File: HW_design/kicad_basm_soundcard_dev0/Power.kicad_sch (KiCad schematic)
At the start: 18 parts, among them J101 USB_C_Receptacle, U101 AMS1117-3.3, U102 AMS1117-3.3

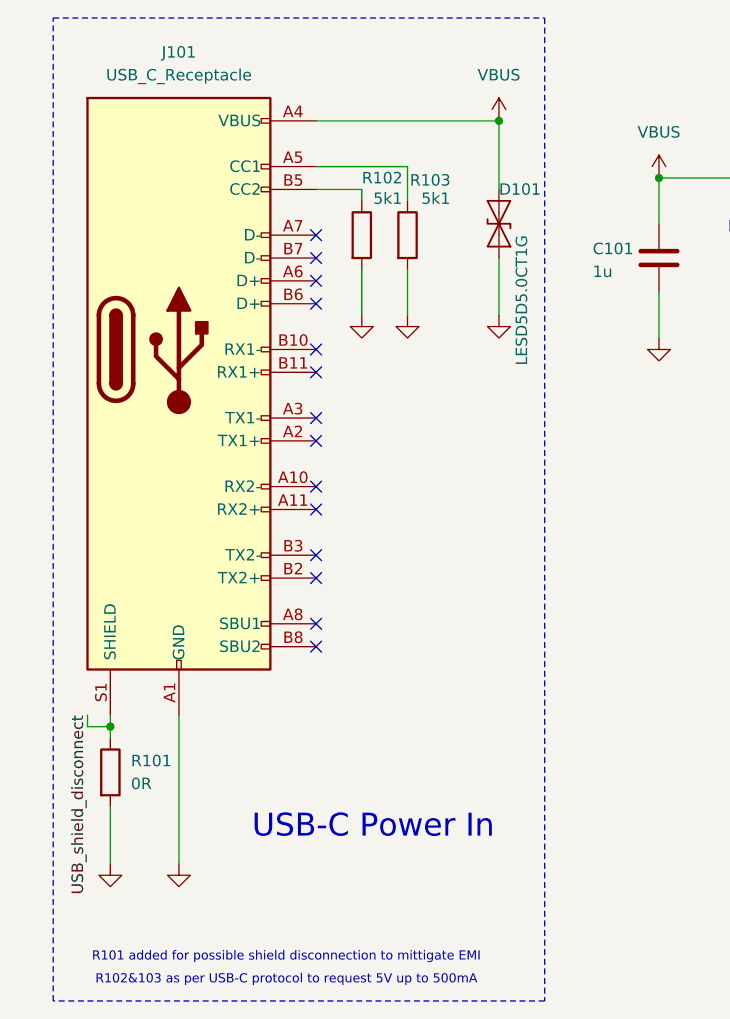
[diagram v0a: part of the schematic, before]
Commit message: Changed Footprints for LED RGB, SD, AudioJack, USB
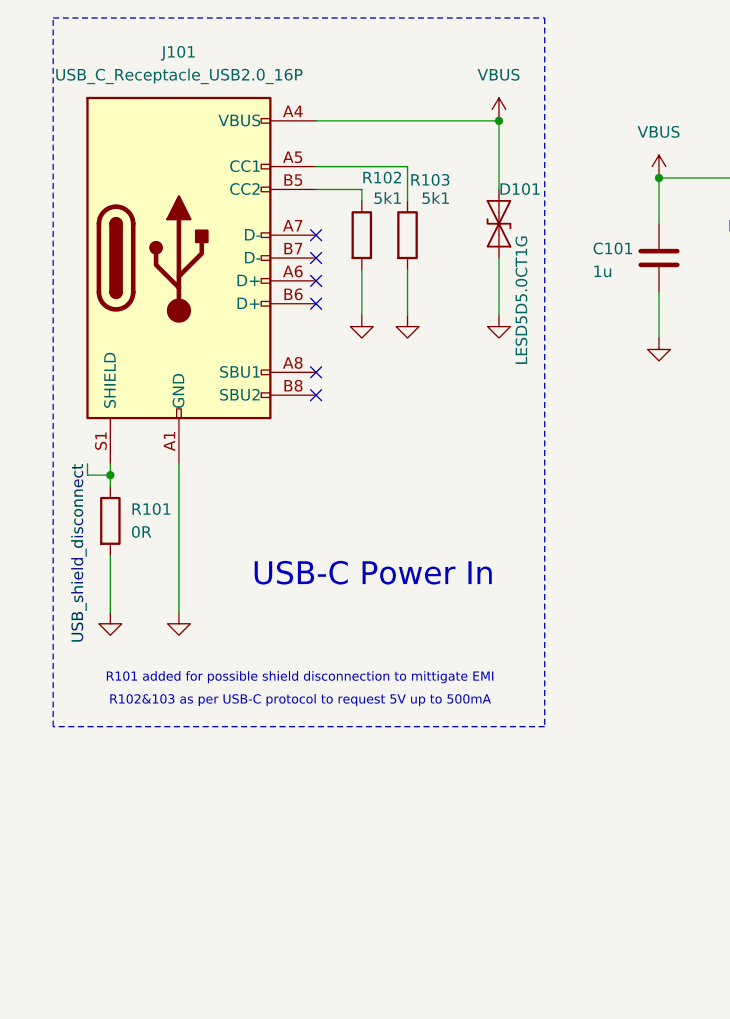
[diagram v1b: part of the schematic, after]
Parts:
- removed J101: USB_C_Receptacle, Connector_USB:USB_C_Receptacle_Molex_105450-0101, symbol Connector:USB_C_Receptacle
- added J101: USB_C_Receptacle_USB2.0_16P, Connector_USB:USB_C_Receptacle_Palconn_UTC16-G, symbol Connector:USB_C_Receptacle_USB2.0_16P
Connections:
- net GND: now also J101.A1 (GND), J101.A12 (GND), J101.B1 (GND), J101.B12 (GND)
- net USB_shield_disconnect: now also J101.S1 (SHIELD)
- net VBUS: now also J101.A4 (VBUS), J101.A9 (VBUS), J101.B4 (VBUS), J101.B9 (VBUS)
- net at R103.1: now also J101.A5 (CC1)
- net at R102.1: now also J101.B5 (CC2)
- no-connect marks 14 -> 6
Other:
- moved on the sheet: R101
